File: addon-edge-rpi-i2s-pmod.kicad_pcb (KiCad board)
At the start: 2 copper layers, 100 x 100 mm, 39 parts, among them J1 PMOD1, J10 Conn_01x02, J12 Conn_01x02, J13 Conn_01x01, J2 PMOD2, J3 PMOD3, J4 PMOD4, J5 Conn_01x06, J6 Conn_01x06, J7 Conn_01x03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

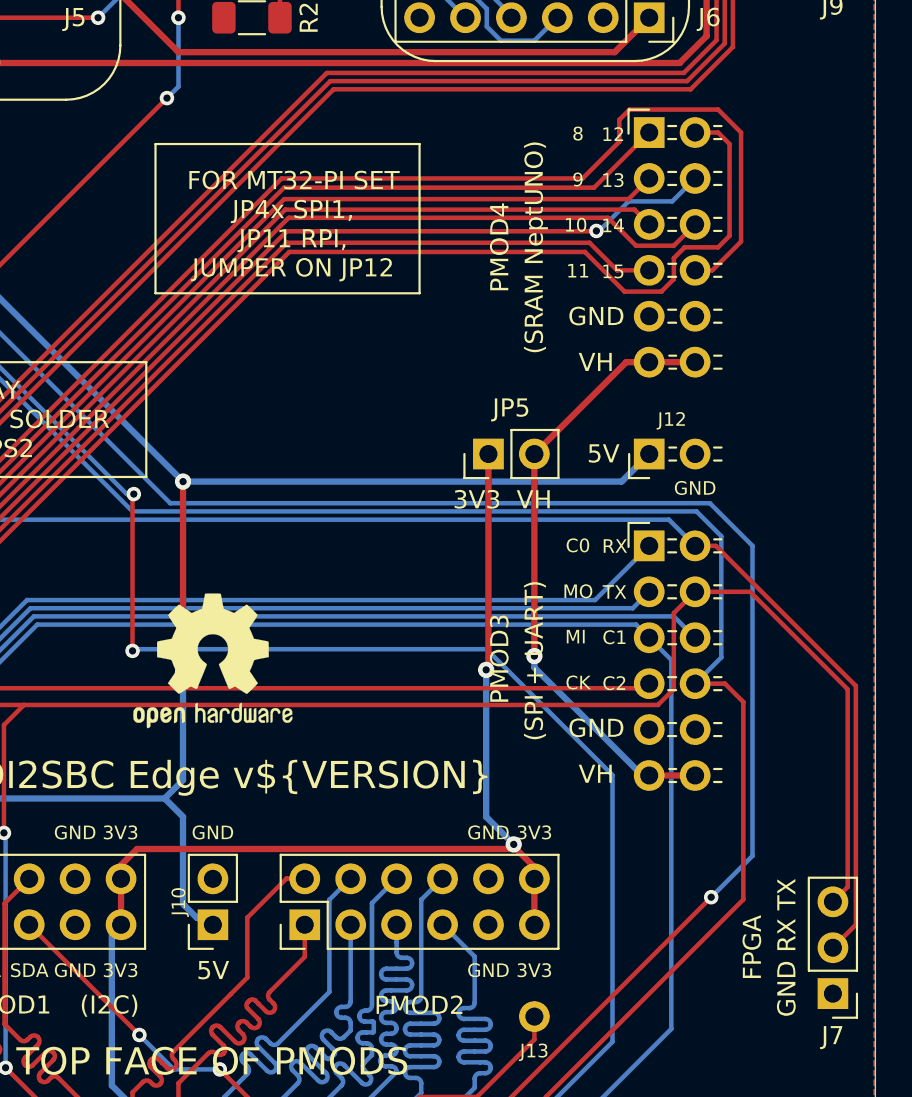
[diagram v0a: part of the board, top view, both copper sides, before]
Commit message: v0.72 silkscreen updated
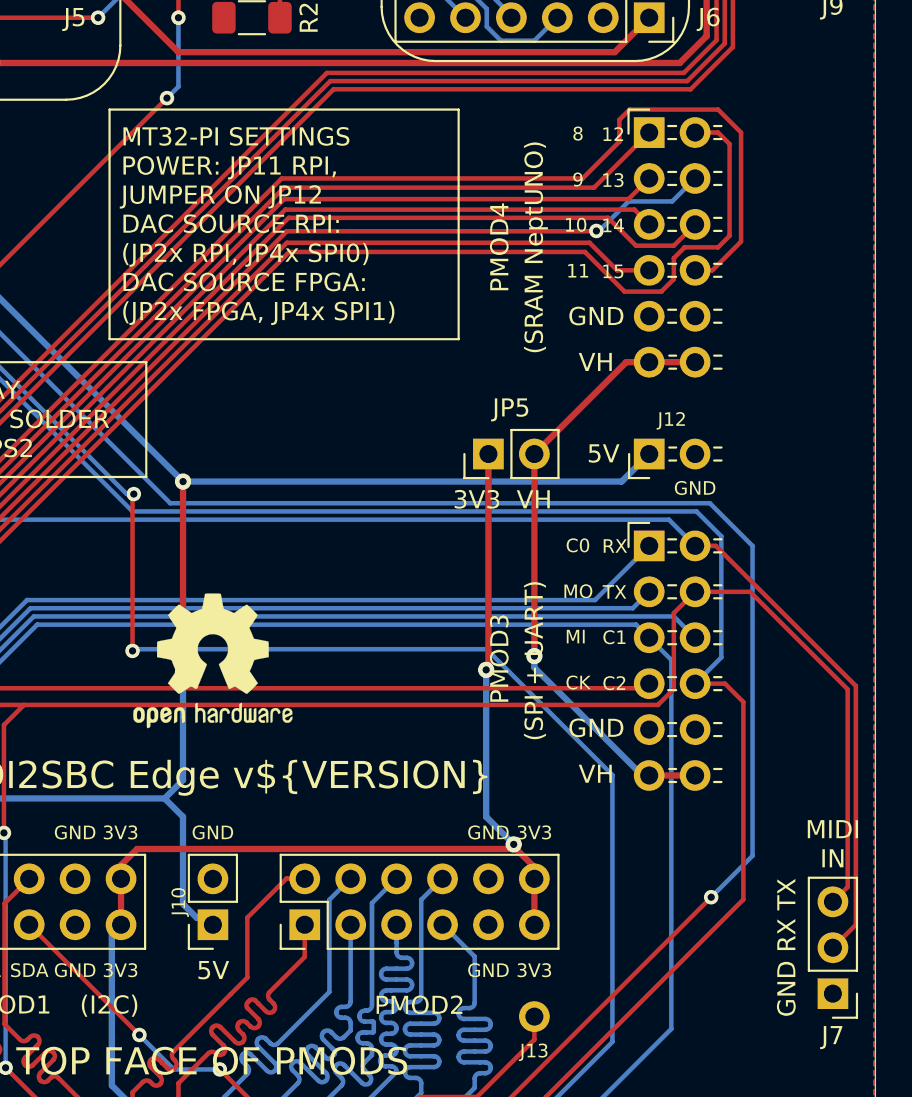
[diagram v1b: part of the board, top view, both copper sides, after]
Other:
- rule pad_to_mask_clearance: 0 -> 0.05
- board text added: "MIDI IN"
- board text added: "MT32-PI SETTINGS POWER: JP11 RPI, JUMPER ON JP12 DAC SOURCE RPI: (JP2x RPI, JP4x SPI0) DAC SOURCE FPGA: (JP2x FPGA, JP4x SPI1)"
- board text removed: "FOR MT32-PI SET JP4x SPI1, JP11 RPI, JUMPER ON JP12"
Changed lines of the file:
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@@
       (dielectric_constraints no)
     )
-    (pad_to_mask_clearance 0)
+    (pad_to_mask_clearance 0.05)
     (pcbplotparams
       (layerselection 0x00010fc_ffffffff)
@@
     )
   )
-  (property "VERSION" "0.71")
+  (property "VERSION" "0.72")
   (net 0 "")
   (net 1 "/B26_WSEL_LRCLK_I2S")
@@
   (gr_line (start 133.985 77.7875) (end 133.35 78.4225) (layer "F.SilkS") (width 0.12))
   (gr_circle (center 149.225 106.045) (end 150.7236 106.045) (layer "F.SilkS") (width 0.12) (fill solid))
-  (gr_rect (start 168.91 85.725) (end 183.515 93.98) (layer "F.SilkS") (width 0.12) (fill none))
+  (gr_rect (start 166.37 83.82) (end 185.674 96.52) (layer "F.SilkS") (width 0.12) (fill none))
   (gr_line (start 127 102.235) (end 127 100.33) (layer "F.SilkS") (width 0.12))
   (gr_line (start 127 100.33) (end 126.365 100.965) (layer "F.SilkS") (width 0.12))
@@
     (effects (font (size 1 1) (thickness 0.15)))
   )
-  (gr_text "FOR MT32-PI SET \nJP4x SPI1,\nJP11 RPI, \nJUMPER ON JP12 " (at 176.53 90.17) (layer "F.SilkS")
-    (effects (font (size 1 1) (thickness 0.15)))
+  (gr_text "MT32-PI SETTINGS\nPOWER: JP11 RPI, \nJUMPER ON JP12\nDAC SOURCE RPI: \n(JP2x RPI, JP4x SPI0)\nDAC SOURCE FPGA: \n(JP2x FPGA, JP4x SPI1)\n" (at 167.005 90.17) (layer "F.SilkS")
+    (effects (font (size 1 1) (thickness 0.15)) (justify left))
   )
   (gr_text "BCLK" (at 116.205 86.36) (layer "F.SilkS")
@@
     (effects (font (size 0.75 0.75) (thickness 0.15)))
   )
-  (gr_text "FPGA" (at 201.93 130.175 90) (layer "F.SilkS")
+  (gr_text "MIDI\nIN" (at 206.375 124.46) (layer "F.SilkS")
     (effects (font (size 1 1) (thickness 0.15)))
   )

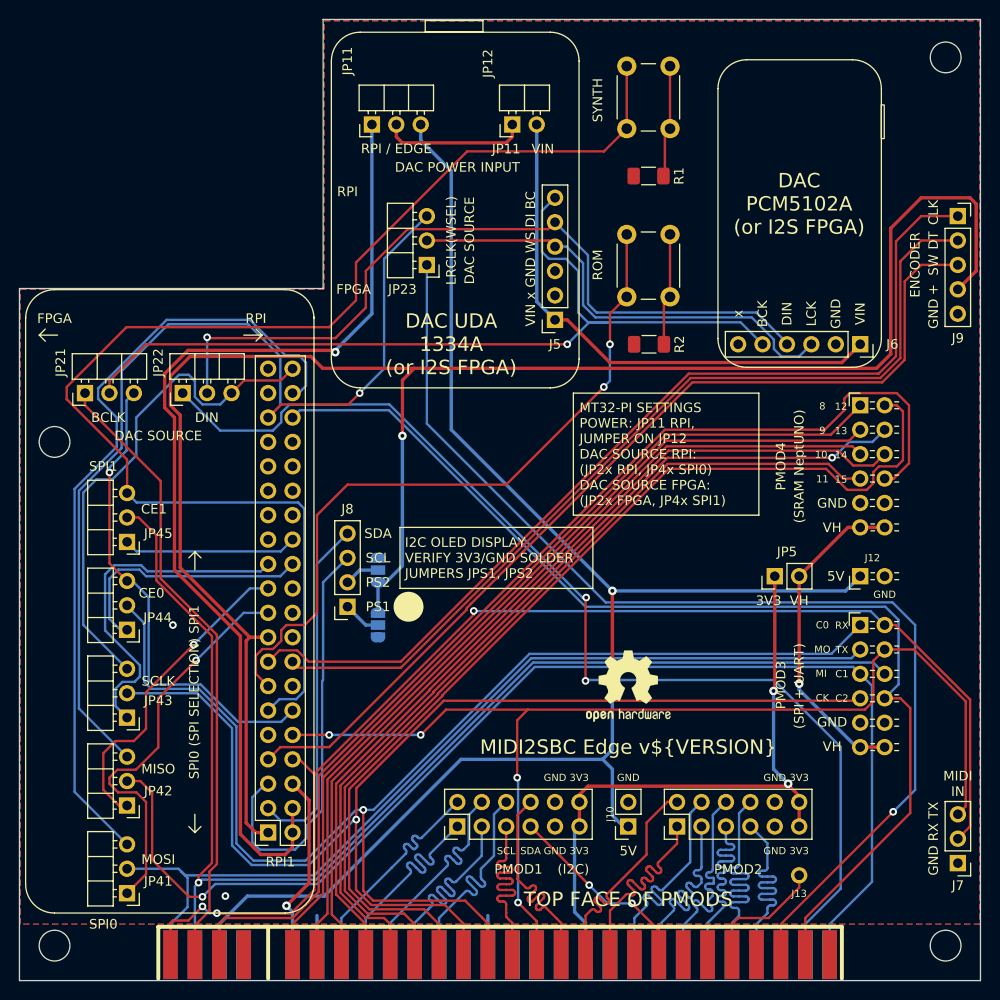
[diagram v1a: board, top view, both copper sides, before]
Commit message: v1.00 minor changes after testing manufactured v0.7
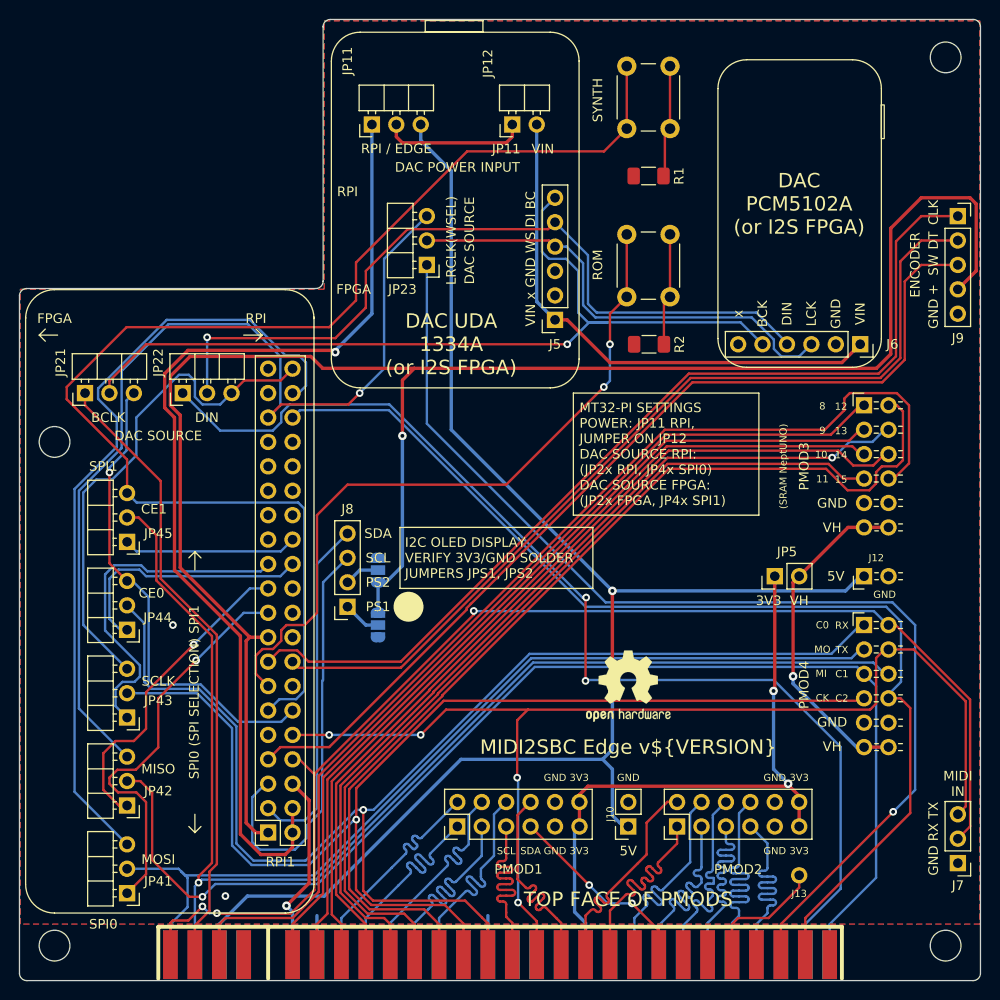
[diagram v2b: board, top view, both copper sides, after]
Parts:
- J3: renamed from J4; value PMOD4 -> PMOD3
- J4: renamed from J3; value PMOD3 -> PMOD4
- moved J12 0.40 mm to (196.6, 102.9)
- moved J3 0.40 mm to (196.6, 97.8)
- moved J4 0.40 mm to (196.6, 120.7)
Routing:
- net /A28_MISO_WSBD: track 127.1 -> 127.7 mm
- net /VH_PMOD: track 34.2 -> 34.7 mm
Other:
- outline, holes or cut-outs redrawn
- board text removed: "(I2C)"
- board text removed: "(SPI + UART)"

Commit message: v1.01 pmod i2s
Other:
- board text added: "(SPI + UART)"
- board text added: "PMOD I2S (REMOVE JP12)"
- board text added: "UART"
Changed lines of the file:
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@@
     )
   )
-  (property "VERSION" "1.00")
+  (property "VERSION" "1.01")
   (net 0 "")
   (net 1 "/B26_WSEL_LRCLK_I2S")
@@
     (fp_line (start 0.49736 29.924) (end 20.26868 29.924) (layer "F.SilkS") (width 0.12))
     (fp_rect (start 7.5 31.14) (end 13.5 29.97) (layer "F.SilkS") (width 0.12) (fill none))
-    (fp_arc (start 23.26868 26.924) (mid 22.39 29.04532) (end 20.26868 29.924) (layer "F.SilkS") (width 0.12))
-    (fp_arc (start 20.26868 -7.076) (mid 22.39 -6.19732) (end 23.26868 -4.076) (layer "F.SilkS") (width 0.12))
+    (fp_arc (start 23.26868 26.924) (mid 22.389999 29.045313) (end 20.26868 29.924) (layer "F.SilkS") (width 0.12))
+    (fp_arc (start 20.26868 -7.076) (mid 22.390013 -6.197327) (end 23.26868 -4.076) (layer "F.SilkS") (width 0.12))
     (fp_arc (start -2.50264 -4.076) (mid -1.62396 -6.19732) (end 0.49736 -7.076) (layer "F.SilkS") (width 0.12))
     (fp_arc (start 0.49736 29.924) (mid -1.62396 29.04532) (end -2.50264 26.924) (layer "F.SilkS") (width 0.12))
@@
   (gr_line (start 110.8075 77.7875) (end 111.4425 78.4225) (layer "F.SilkS") (width 0.12))
   (gr_line (start 208.725 45.7117) (end 208.725 144.17675) (layer "Edge.Cuts") (width 0.05))
-  (gr_arc (start 109.512 144.93875) (mid 108.973185 144.715565) (end 108.75 144.17675) (layer "Edge.Cuts") (width 0.05))
   (gr_arc (start 140.335 45.7117) (mid 140.558185 45.172885) (end 141.097 44.9497) (layer "Edge.Cuts") (width 0.05))
+  (gr_arc (start 109.512 144.93875) (mid 108.973185 144.715565) (end 108.75 144.17675) (layer "Edge.Cuts") (width 0.05))
   (gr_arc (start 140.335 72.1767) (mid 140.111815 72.715515) (end 139.573 72.9387) (layer "Edge.Cuts") (width 0.05))
   (gr_line (start 141.097 44.9497) (end 207.963 44.9497) (layer "Edge.Cuts") (width 0.05))
@@
     (effects (font (size 1 1) (thickness 0.15)))
   )
+  (gr_text "(SPI + UART)" (at 188.214 114.3 90) (layer "F.SilkS")
+    (effects (font (size 0.75 0.75) (thickness 0.15)))
+  )
   (gr_text "+" (at 203.835 73.025) (layer "F.SilkS")
     (effects (font (size 1 1) (thickness 0.15)))
@@
     (effects (font (size 1 1) (thickness 0.15)))
   )
+  (gr_text "UART" (at 202.057 130.175 90) (layer "F.SilkS")
+    (effects (font (size 1 1) (thickness 0.15)))
+  )
   (gr_text "MIDI2SBC Edge v${VERSION}\n" (at 172.085 120.65) (layer "F.SilkS")
     (effects (font (size 1.5 1.5) (thickness 0.15)))
@@
     (effects (font (size 1.5 1.5) (thickness 0.15)))
   )
+  (gr_text "PMOD I2S\n(REMOVE JP12)" (at 190.5 71.882) (layer "F.SilkS")
+    (effects (font (size 1 1) (thickness 0.15)))
+  )
   (gr_text "GND RX TX" (at 203.835 130.175 90) (layer "F.SilkS")

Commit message: v1.02 minor silkscreen updates
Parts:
- moved JP23 0.65 mm to (151.1, 69.8)
- moved R2 0.51 mm to (174.2, 78.2)
- moved R1 0.51 mm to (174.2, 60.7)
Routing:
- net /A28_SPI1_MISO_WSBD: track 102.7 -> 103.7 mm
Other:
- board text added: "DAC PCM5102A"
- board text added: "DAC UDA 1334A"
- board text added: "I2S FPGA"
- board text added: "PMOD I2S FPGA (REMOVE JP12)"
- board text removed: "DAC PCM5102A (or I2S FPGA)"
- board text removed: "DAC UDA 1334A (or I2S FPGA)"
- board text removed: "PMOD I2S (REMOVE JP12)"
